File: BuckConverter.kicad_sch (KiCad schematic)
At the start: 12 parts, among them U1 TPS62133, U2 APH0630T2R2M, U3 AMS1117-3.3

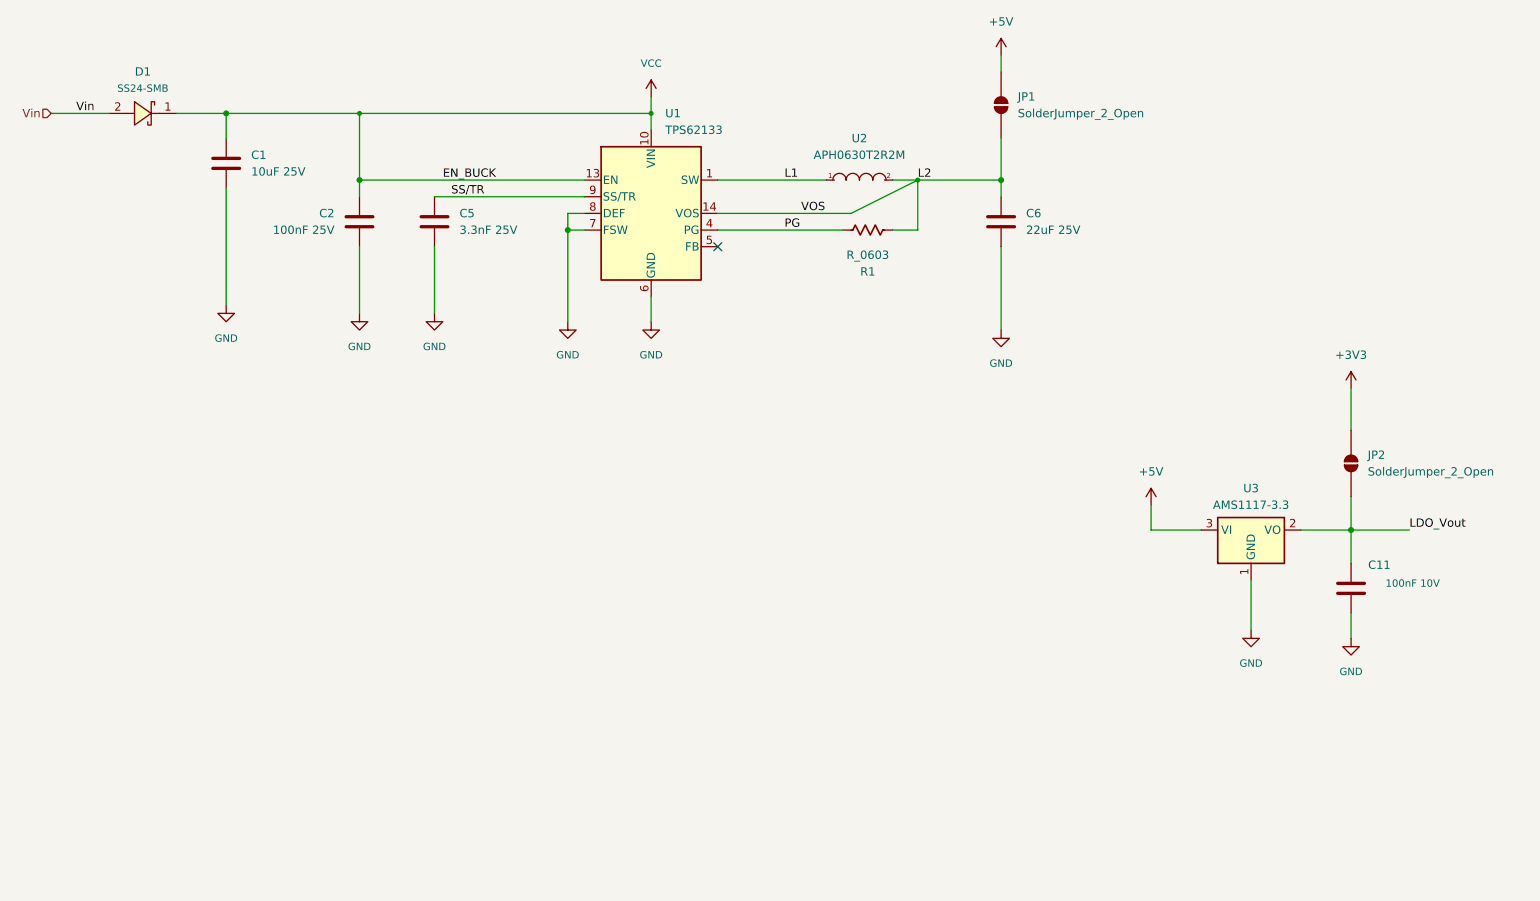
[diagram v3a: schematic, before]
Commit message: asignacion de huellas, valores y lcsc part #, dejar de rastrear .history/
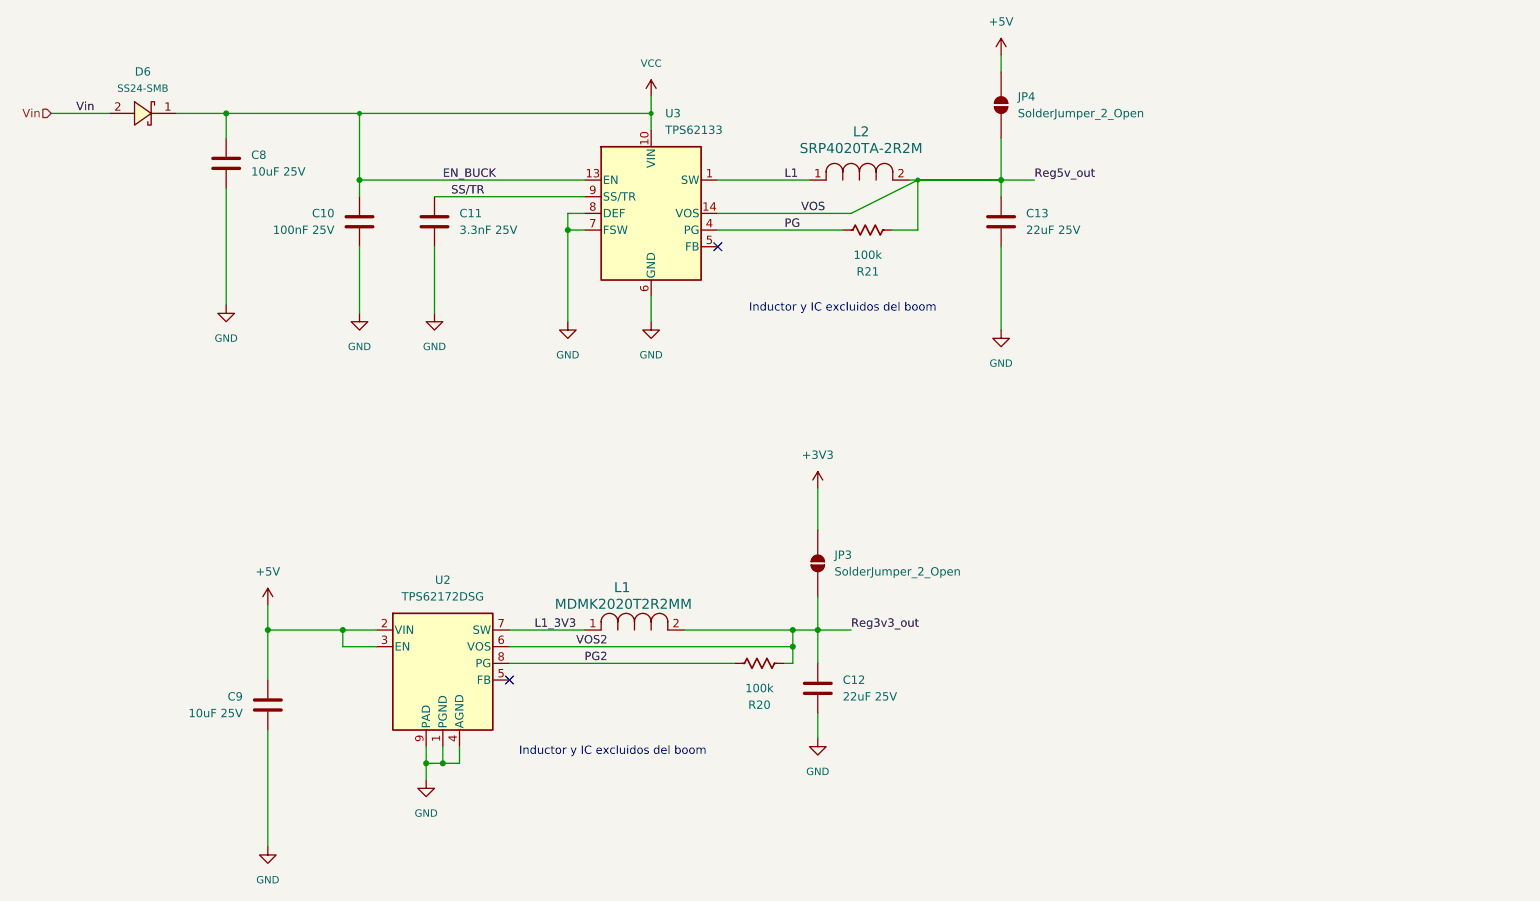
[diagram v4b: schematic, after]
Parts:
- removed C11: 100nF 10V, PCM_Capacitor_SMD_AKL:C_0603_1608Metric, symbol PCM_Capacitor_US_AKL:C_0603
- removed U2: APH0630T2R2M, EasyEDA:IND-SMD_L7.0-W6.6_MCW-0650-220, symbol EasyEDA:L_7x6.6mm SMD
- removed U3: AMS1117-3.3, Package_TO_SOT_SMD:SOT-223-3_TabPin2, symbol Regulator_Linear:AMS1117-3.3
- added C12: 22uF 25V, PCM_Capacitor_SMD_AKL:C_0805_2012Metric, symbol PCM_Capacitor_US_AKL:C_0805
- added C9: 10uF 25V, PCM_Capacitor_SMD_AKL:C_1210_3225Metric, symbol PCM_Capacitor_US_AKL:C_1210
- added L1: MDMK2020T2R2MM, Snapeda:IND_MDMK2020T1R0MM_TAY, symbol Snapeda:MDMK2020T2R2MM
- added L2: SRP4020TA-2R2M, Snapeda:IND_SRP4020TA_BRN-L, symbol Snapeda:SRP4020TA-2R2M
- added R20: 100k, PCM_Resistor_SMD_AKL:R_0603_1608Metric, symbol PCM_Resistor_US_AKL:R_0603
- added U2: TPS62172DSG, Package_SON:WSON-8-1EP_2x2mm_P0.5mm_EP0.9x1.6mm_ThermalVias, symbol Regulator_Switching:TPS62172DSG
- C10: renamed from C2; LCSC Part (none) -> C14663
- C11: renamed from C5; LCSC Part (none) -> C107088
- C13: renamed from C6; LCSC Part (none) -> C602037
- C8: renamed from C1; LCSC Part (none) -> C577292
- JP3: renamed from JP2; footprint (none) -> PCM_SparkFun-Jumper:Jumper_2_NO
- JP4: renamed from JP1; footprint (none) -> PCM_SparkFun-Jumper:Jumper_2_NO
- R21: renamed from R1; value R_0603 -> 100k; LCSC Part (none) -> C122538
- U3: renamed from U1; now left out of the parts list
- renumbered D1 to D6
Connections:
- net +5V: now also C9.1, U2.2 (VIN), U2.3 (EN)
- net GND: now also C12.2, C9.2, U2.1 (PGND), U2.4 (AGND), U2.9 (PAD)
- net L1: now also L2.1
- net L2 renamed Reg5v_out
- net Reg5v_out: now also L2.2
- net LDO_Vout renamed Reg3v3_out
- net Reg3v3_out: now also C12.1, L1.2, R20.1, U2.6 (VOS)
- new net L1_3V3: L1.1, U2.7 (SW)
- new net PG2: R20.2, U2.8 (PG)
- no-connect marks 1 -> 2
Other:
- note added: "Inductor y IC excluidos del boom"
- moved on the sheet: JP3

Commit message: pcb desing done, add productions files
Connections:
- net PG2: now also R20.1; no longer R20.2
- net Reg3v3_out: now also R20.2; no longer R20.1
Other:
- note added: "2.2uH up to 0.5A 2Mhz"
- note added: "2.2uH up to 4A 2Mhz"
- moved on the sheet: R20
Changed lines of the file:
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@@
 	(generator_version "10.0")
 	(paper "USLedger")
+	(text "2.2uH up to 0.5A\n2Mhz"
+		(exclude_from_sim no)
+		(at 215.138 148.59 0)
+		(effects
+			(font
+				(size 1.27 1.27)
+			)
+		)
+	)
 	(text "Inductor y IC excluidos del boom"
 		(exclude_from_sim no)
@@
 		(exclude_from_sim no)
 		(at 212.598 178.562 0)
+		(effects
+			(font
+				(size 1.27 1.27)
+			)
+		)
+	)
+	(text "2.2uH up to 4A\n2Mhz"
+		(exclude_from_sim no)
+		(at 248.412 80.264 0)
 		(effects
 			(font
@@
 	(symbol
 		(lib_id "PCM_Resistor_US_AKL:R_0603")
-		(at 234.95 165.1 270)
+		(at 234.95 165.1 90)
 		(unit 1)
 		(body_style 1)
@@
 		(dnp no)
 		(property "Reference" "R20"
-			(at 234.95 171.45 90)
+			(at 234.95 158.75 90)
 			(show_name no)
 			(do_not_autoplace no)
@@
 		)
 		(property "Value" "100k"
-			(at 234.95 168.91 90)
+			(at 234.95 161.29 90)
 			(show_name no)
 			(do_not_autoplace no)
@@
 		)
 		(property "Footprint" "PCM_Resistor_SMD_AKL:R_0603_1608Metric"
-			(at 223.52 165.1 0)
-			(hide yes)
-			(show_name no)
+			(at 246.38 165.1 0)
+			(hide yes)
+			(show_name no)

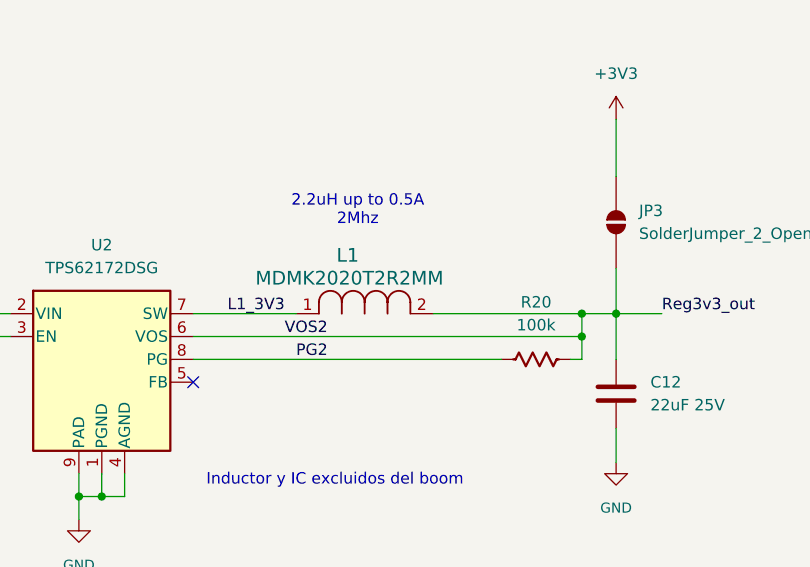
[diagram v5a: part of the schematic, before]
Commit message: cambiar bobina de power suppy
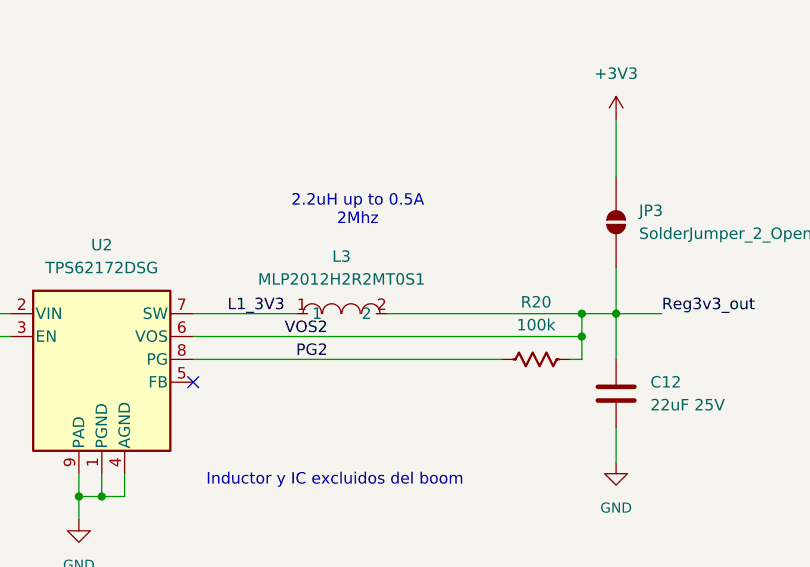
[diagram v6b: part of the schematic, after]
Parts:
- removed L1: MDMK2020T2R2MM, Snapeda:IND_MDMK2020T1R0MM_TAY, symbol Snapeda:MDMK2020T2R2MM
- added L3: MLP2012H2R2MT0S1, EasyEDA:L0805, symbol EasyEDA:MLP2012H2R2MT0S1
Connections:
- net L1_3V3: now also L3.1
- net Reg3v3_out: now also L3.2
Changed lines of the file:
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@@
+	(wire
+		(pts
+			(xy 218.44 160.02) (xy 240.03 160.02)
+		)
+		(stroke
+			(width 0.508)
+			(type default)
+		)
+	)
 	(wire
 		(pts
@@
 		(pts
 			(xy 171.45 160.02) (xy 176.53 160.02)
-		)
-		(stroke
-			(width 0.508)
-			(type default)
-		)
-	)
-	(wire
-		(pts
-			(xy 223.52 160.02) (xy 240.03 160.02)
 		)
 		(stroke
@@
 	)
 	(symbol
+		(lib_id "EasyEDA:MLP2012H2R2MT0S1")
+		(at 213.36 160.02 0)
+		(unit 1)
+		(body_style 1)
+		(exclude_from_sim no)
+		(in_bom yes)
+		(on_board yes)
+		(in_pos_files yes)
+		(dnp no)
+		(fields_autoplaced yes)
+		(property "Reference" "L3"
+			(at 213.33 153.67 0)
+			(show_name no)
+			(do_not_autoplace no)
+			(effects
+				(font
+					(size 1.27 1.27)
+				)
+			)
+		)
+		(property "Value" "MLP2012H2R2MT0S1"
+			(at 213.33 156.21 0)
+			(show_name no)
+			(do_not_autoplace no)
+			(effects
+				(font
+					(size 1.27 1.27)
+				)
+			)
+		)
+		(property "Footprint" "EasyEDA:L0805"
+			(at 213.36 167.64 0)
+			(hide yes)
+			(show_name no)
+			(do_not_autoplace no)
+			(effects
+				(font
+					(size 1.27 1.27)
+				)
+			)
+		)
+		(property "Datasheet" "https://lcsc.com/product-detail/presales_TDK-MLP2012H2R2MT0S1_C383369.html"
+			(at 213.36 170.18 0)
+			(hide yes)
+			(show_name no)
+			(do_not_autoplace no)
+			(effects
+				(font
+					(size 1.27 1.27)
+				)
+			)
+		)
+		(property "Description" ""
+			(at 213.36 160.02 0)
+			(hide yes)
+			(show_name no)
+			(do_not_autoplace no)
+			(effects
+				(font
+					(size 1.27 1.27)
+				)
+			)
+		)
+		(property "Manufacturer" "TDK"
+			(at 213.36 172.72 0)
+			(hide yes)
+			(show_name no)
+			(do_not_autoplace no)
+			(effects
+				(font
+					(size 1.27 1.27)
+				)
+			)
+		)
+		(property "MPN" "MLP2012H2R2MT0S1"
+			(at 213.36 175.26 0)
+			(hide yes)
+			(show_name no)
+			(do_not_autoplace no)
+			(effects
+				(font
+					(size 1.27 1.27)
+				)
+			)
+		)
+		(property "LCSC Part" "C383369"
+			(at 213.36 177.8 0)
+			(hide yes)
+			(show_name no)
+			(do_not_autoplace no)
+			(effects
+				(font
+					(size 1.27 1.27)
+				)
+			)
+		)
+		(pin "1"
+		)
+		(pin "2"
+		)
+		(instances
+			(project "USAR_Drone_Feature"
+				(path "/b3437995-bb94-4c2f-9ed8-b1af477fe956/bbae36a6-1608-41fb-8b94-fa07ee9e7141"
+					(reference "L3")
+					(unit 1)
+				)
+			)
+		)
+	)
+	(symbol
 		(lib_id "power:GND")
 		(at 185.42 111.76 0)
@@
 					(unit 1)
 				)
-			)
-		)
-	)
-	(symbol
-		(lib_id "Snapeda:MDMK2020T2R2MM")
-		(at 216.535 167.005 0)
-		(mirror y)
-		(unit 1)
-		(body_style 1)
-		(exclude_from_sim no)
-		(in_bom no)
-		(on_board yes)
-		(in_pos_files yes)
-		(dnp no)
-		(property "Reference" "L1"
-			(at 215.265 153.543 0)
-			(show_name no)
-			(do_not_autoplace no)
-			(effects
-				(font
-					(size 1.524 1.524)
-				)
-				(justify left)
-			)
-		)
-		(property "Value" "MDMK2020T2R2MM"
-			(at 224.663 156.083 0)
-			(show_name no)
-			(do_not_autoplace no)
-			(effects
-				(font
-					(size 1.524 1.524)
-				)
-				(justify left)
-			)
-		)
-		(property "Footprint" "Snapeda:IND_MDMK2020T1R0MM_TAY"
-			(at 215.265 160.6549 0)
-			(hide yes)
-			(show_name no)
-			(do_not_autoplace no)
-			(effects
-				(font
-					(size 1.27 1.27)
-				)
-				(justify left)
-			)
-		)
-		(property "Datasheet" "MDMK2020T2R2MM"
-			(at 215.265 163.1949 0)
-			(hide yes)
-			(show_name no)
-			(do_not_autoplace no)
-			(effects
-				(font
-					(size 1.27 1.27)
-				)
-				(justify left)
-			)
-		)
-		(property "Description" ""
-			(at 216.535 167.005 0)
-			(hide yes)
-			(show_name no)
-			(do_not_autoplace no)
-			(effects
-				(font
-					(size 1.27 1.27)
-				)
-			)
-		)
-		(pin "1"
-		)
-		(pin "2"
-		)
-		(instances
-			(project "USAR_Drone_Feature"
-				(path "/b3437995-bb94-4c2f-9ed8-b1af477fe956/bbae36a6-1608-41fb-8b94-fa07ee9e7141"
-					(reference "L1")
-					(unit 1)
-				)
